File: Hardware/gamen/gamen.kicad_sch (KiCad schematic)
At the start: 1 part, among them U1 STM32H743IGTx

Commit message: Gamen: Power supply done and mcu basics done in shcems with minor fix in shori
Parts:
- removed U1: STM32H743IGTx, Package_QFP:LQFP-176_24x24mm_P0.5mm, symbol MCU_ST_STM32H7:STM32H743IGTx
- added C1, C2, C24, C25: 10uF, symbol Device:C
- added C10, C11, C13, C14, C15, C16, C17, C18, C19, C20, C21, C22, C23, C26, C28, C3, C32, C7, C8, C9: 100nF, symbol Device:C
- added C12: 100nF, Capacitor_SMD:C_0402_1005Metric_Pad0.74x0.62mm_HandSolder, symbol Device:C
- added C27, C31: 1uF, symbol Device:C
- added C29, C30: 2.2uF, symbol Device:C
- added C4: 22uF, symbol Device:C
- added C5, C6: 12pF, symbol Device:C
- added J1: POWER IN, symbol Connector_Generic:Conn_01x02
- added L1: 3.3uH, symbol Device:L
- added R1: 33.2K, symbol Device:R
- added R2, R3: 10K, symbol Device:R
- added R4: 10Ω, symbol Device:R
- added RST1: SW_Push, Button_Switch_SMD:SW_SPST_B3U-1000P, symbol Switch:SW_Push
- added SW1: SW_SPDT, Connector_PinHeader_2.54mm:PinHeader_1x03_P2.54mm_Vertical, symbol Switch:SW_SPDT
- added U1: TPS562201DDCR, Package_TO_SOT_SMD:SOT-23-6, symbol My symbols:TPS62086RLTR
- added U2: STM32H743IITx, Package_QFP:LQFP-176_24x24mm_P0.5mm, symbol MCU_ST_STM32H7:STM32H743IITx
- added Y1: 25MHz, Crystal:Crystal_SMD_WE_CFPX-180-4Pin_3.2x2.5mm, symbol Device:Crystal_GND2
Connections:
- new net: C29.1, U2.125 (VCAP)
- new net: R3.1, U2.166 (BOOT0)
- new net: C30.1, U2.81 (VCAP)
- new net: C3.2, L1.1, U1.2 (SW)
- new net: C3.1, U1.6 (VBST)
- new net: R1.2, R2.1, U1.4 (VFB)
- new net +3.3V: C10.2, C11.2, C13.2, C14.2, C15.2, C16.1, C17.1, C18.1, C19.1, C20.1, C21.1, C22.1, C23.1, C24.1, C4.1, C7.2, C8.2, C9.2, L1.2, R1.1, R4.1, SW1.3 (C), U2.103 (VDD), U2.114 (VDD33_USB), U2.127 (VDD), U2.136 (VDD), U2.149 (VDD), U2.15 (VDD), U2.159 (VDD), U2.172 (VDD), U2.23 (VDD), U2.36 (VDD), U2.49 (VDD), U2.6 (VBAT), U2.62 (VDD), U2.72 (VDD), U2.82 (VDD), U2.91 (VDD)
- new net +3.3VA: C25.1, C26.1, C27.1, C28.1, C31.1, C32.1, R4.2, U2.38 (VREF+), U2.39 (VDDA)
- new net +5V: C1.1, C2.1, J1.2 (Pin_2), U1.3 (VIN), U1.5 (EN)
- new net BOOT0_R_TO_SW: R3.2, SW1.2 (B)
- new net GND: C1.2, C10.1, C11.1, C12.2, C13.1, C14.1, C15.1, C16.2, C17.2, C18.2, C19.2, C2.2, C20.2, C21.2, C22.2, C23.2, C24.2, C25.2, C26.2, C27.2, C28.2, C29.2, C30.2, C31.2, C32.2, C4.2, C5.2, C6.2, C7.1, C8.1, C9.1, J1.1 (Pin_1), R2.2, RST1.2, SW1.1 (A), U1.1 (GND), U2.102 (VSS), U2.113 (VSS), U2.126 (VSS), U2.135 (VSS), U2.14 (VSS), U2.148 (VSS), U2.158 (VSS), U2.22 (VSS), U2.37 (VSSA), U2.48 (VSS), U2.61 (VSS), U2.71 (VSS), U2.90 (VSS), Y1.2
- new net NRST: C12.1, RST1.1, U2.31 (NRST)
- new net OSC_IN: C5.1, U2.29 (PH0), Y1.3
- new net OSC_OUT: C6.1, U2.30 (PH1), Y1.1
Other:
- note added: "POWER SUPPLY"

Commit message: GAMEN: Started SDRAM
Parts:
- added C33: 100nF, Capacitor_SMD:C_0402_1005Metric_Pad0.74x0.62mm_HandSolder, symbol Device:C
- added C34, C35, C36, C37, C38, C39, C40, C41, C42: 100nF, symbol Device:C
- added C43: 10uF, symbol Device:C
- added J2: Conn_01x05_Pin, Connector_Molex:Molex_PicoBlade_53048-0510_1x05_P1.25mm_Horizontal, symbol Connector:Conn_01x05_Pin
- added J3: UART_Header, MyFootprints:CONN04_530480410_MOL, symbol Connector:Conn_01x04_Pin
- added U14: (no value), Package_TO_SOT_SMD:SOT-23, symbol MyCrystal:ESDS452DBZRQ1
- added U3: AS4C16M16SA-6TIN, Package_SO:TSOP-II-54_22.2x10.16mm_P0.8mm, symbol My symbols:AS4C16M16SA-6TIN
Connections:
- net +3.3V: now also C33.1, C34.1, C35.2, C36.2, C37.2, C38.2, C39.2, C40.2, C41.2, C42.2, C43.2, J2.5 (Pin_5), J3.1 (Pin_1), U3.1 (VDD), U3.14 (VDD), U3.27 (VDD), U3.3 (VDDQ), U3.43 (VDDQ), U3.49 (VDDQ), U3.9 (VDDQ)
- net GND: now also C33.2, C34.2, C35.1, C36.1, C37.1, C38.1, C39.1, C40.1, C41.1, C42.1, C43.1, J2.1 (Pin_1), J3.4 (Pin_4), U14.3 (GND), U3.12 (VSSQ), U3.28 (VSS), U3.41 (VSS), U3.46 (VSSQ), U3.52 (VSSQ), U3.54 (VSS), U3.6 (VSSQ)
- net NRST: now also J2.2 (Pin_2)
- net SWDIO: now reaches U2.124 (PA13)
- net SWDIO: now also J2.4 (Pin_4)
- net SWCLK: now reaches U2.137 (PA14)
- net SWCLK: now also J2.3 (Pin_3)
- net BOOT0: now reaches R3.1, U2.166 (BOOT0)
- new net SDRAM_DQ0: U3.2 (DQ0)
- new net UART_RX: J3.2 (Pin_2), U14.2 (IO2)
- new net UART_TX: J3.3 (Pin_3)
- no-connect marks 0 -> 1
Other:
- note added: "UART SWITCH ON GAMEN"
- moved on the sheet: C10, C11, C12, C13, C14, C15, C16, C17, C18, C19, C20, C21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

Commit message: Gamen: Screen FPC connector added
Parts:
- added C44: 10uF, symbol Device:C
- added C45: 100nF, symbol Device:C
- added J4: MIDI CONN, Connector_Molex:Molex_PicoBlade_53048-0210_1x02_P1.25mm_Horizontal, symbol Connector_Generic:Conn_01x02
- added J5: SCREEN CONN, symbol Connector_Generic:Conn_01x40
- added R5: 220Ω, symbol Device:R
- added U4: W25Q256JWPIQ, Package_SON:WSON-8-1EP_6x5mm_P1.27mm_EP3.4x4.3mm, symbol Memory_Flash:W25Q128JVP
- added U6: (no value), Package_TO_SOT_SMD:SOT-23, symbol MyCrystal:ESDS452DBZRQ1
- added U7: TLP2361(E, Package_SO:SO-5-6_4.55x3.7mm_P1.27mm, symbol Isolator:TLP2310
- renumbered U14 to U5
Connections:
- net +3.3V: now also C44.2, C45.2, J5.4 (Pin_4), U4.8 (VCC), U7.6 (VDD)
- net +5V: now also J5.1 (Pin_1), J5.2 (Pin_2), U6.1 (IO1), U6.2 (IO2)
- net GND: now also C44.1, C45.1, J5.29 (Pin_29), J5.3 (Pin_3), J5.36 (Pin_36), U4.4 (GND), U4.9 (EP), U6.3 (GND), U7.4 (GND)
- net SDRAM_DQ0: now also U2.104 (PD14), U2.142 (PD0)
- net UART_RX: now also J3.3 (Pin_3), U2.93 (PB13); no longer J3.2 (Pin_2)
- net UART_TX: now also J3.2 (Pin_2), U2.92 (PB12), U5.1 (IO1); no longer J3.3 (Pin_3)
- net SDRAM_DQ1: now reaches U2.105 (PD15)
- net SDRAM_DQ1: now also U3.4 (DQ1)
- net SDRAM_A12: now reaches U2.106 (PG2)
- net SDRAM_A12: now also U3.36 (A12)
- net SDRAM_BA0: now reaches U2.108 (PG4)
- net SDRAM_BA0: now also U3.20 (BA0)
- net SDRAM_BA1: now reaches U2.109 (PG5)
- net SDRAM_BA1: now also U3.21 (BA1)
- net SDRAM_CLK: now reaches U2.112 (PG8)
- net SDRAM_CLK: now also U3.38 (CLK)
- net SDRAM_DQ3: now reaches U2.143 (PD1)
- net SDRAM_DQ3: now also U3.7 (DQ3)
- net SDRAM_A0: now reaches U2.16 (PF0)
- net SDRAM_A0: now also U3.23 (A0)
- net SDRAM_CAS: now reaches U2.160 (PG15)
- net SDRAM_CAS: now also U3.17 (*CAS)
- net SDRAM_NBL0: now reaches U2.169 (PE0)
- net SDRAM_NBL0: now also U3.15 (LDQM)
- net SDRAM_A1: now reaches U2.17 (PF1)
- net SDRAM_A1: now also U3.24 (A1)
- net SDRAM_NBL1: now reaches U2.170 (PE1)
- net SDRAM_NBL1: now also U3.39 (UDQM)
- net SDRAM_A2: now reaches U2.18 (PF2)
- net SDRAM_A2: now also U3.25 (A2)
- net SDRAM_A3: now reaches U2.19 (PF3)
- net SDRAM_A3: now also U3.26 (A3)
- net SDRAM_A4: now reaches U2.20 (PF4)
- net SDRAM_A4: now also U3.29 (A4)
- net SDRAM_A5: now reaches U2.21 (PF5)
- net SDRAM_A5: now also U3.30 (A5)
- net QSPI_IO3: now reaches U2.24 (PF6)
- net QSPI_IO3: now also U4.7 (~{HOLD}/~{RESET}/IO_{3})
- net QSPI_IO2: now reaches U2.25 (PF7)
- net QSPI_IO2: now also U4.3 (~{WP}/IO_{2})
- net QSPI_IO1: now reaches U2.26 (PF8)
- net QSPI_IO1: now also U4.2 (DO/IO_{1})
- net QSPI_IO0: now reaches U2.27 (PF9)
- net QSPI_IO0: now also U4.5 (DI/IO_{0})
- net QSPI_CLK: now reaches U2.28 (PF10)
- net QSPI_CLK: now also U4.6 (CLK)
- net SDRAM_WE: now reaches U2.32 (PC0)
- net SDRAM_WE: now also U3.16 (*WE)
- net SDRAM_CS: now reaches U2.34 (PC2_C)
- net SDRAM_CS: now also U3.19 (*CS)
- net SDRAM_CKE: now reaches U2.35 (PC3_C)
- net SDRAM_CKE: now also U3.37 (CKE)
- net SDNIS_RAS: now reaches U2.59 (PF11)
- net SDNIS_RAS: now also U3.18 (*RAS)
- net SDRAM_A6: now reaches U2.60 (PF12)
- net SDRAM_A6: now also U3.31 (A6)
- net SDRAM_A7: now reaches U2.63 (PF13)
- net SDRAM_A7: now also U3.32 (A7)
- net SDRAM_A8: now reaches U2.64 (PF14)
- net SDRAM_A8: now also U3.33 (A8)
- net SDRAM_A9: now reaches U2.65 (PF15)
- net SDRAM_A9: now also U3.34 (A9)
- net SDRAM_A10: now reaches U2.66 (PG0)
- net SDRAM_A10: now also U3.22 (A10/AP)
- net SDRAM_A11: now reaches U2.67 (PG1)
- net SDRAM_A11: now also U3.35 (A11)
- net SDRAM_DQ6: now reaches U2.68 (PE7)
- net SDRAM_DQ6: now also U3.11 (DQ6)
- net SDRAM_DQ5: now reaches U2.69 (PE8)
- net SDRAM_DQ5: now also U3.10 (DQ5)
- net SDRAM_DQ4: now reaches U2.70 (PE9)
- net SDRAM_DQ4: now also U3.8 (DQ4)
- net SDRAM_DQ7: now reaches U2.73 (PE10)
- net SDRAM_DQ7: now also U3.13 (DQ7)
- net SDRAM_DQ8: now reaches U2.74 (PE11)
- net SDRAM_DQ8: now also U3.42 (DQ8)
- net SDRAM_DQ9: now reaches U2.75 (PE12)
- net SDRAM_DQ9: now also U3.44 (DQ9)
- net SDRAM_DQ10: now reaches U2.76 (PE13)
- net SDRAM_DQ10: now also U3.45 (DQ10)
- net SDRAM_DQ11: now reaches U2.77 (PE14)
- net SDRAM_DQ11: now also U3.47 (DQ11)
- net SDRAM_DQ12: now reaches U2.78 (PE15)
- net SDRAM_DQ12: now also U3.48 (DQ12)
- net SDRAM_DQ13: now reaches U2.96 (PD8)
- net SDRAM_DQ13: now also U3.50 (DQ13)
- net SDRAM_DQ14: now reaches U2.97 (PD9)
- net SDRAM_DQ14: now also U3.51 (DQ14)
- net SDRAM_DQ15: now reaches U2.98 (PD10)
- net SDRAM_DQ15: now also U3.53 (DQ15)
- net SDRAM_DQ2: now reaches U3.5 (DQ2)
- new net: R5.2, U7.1 (A)
- new net MIDI_GND: J4.1 (Pin_1), U7.3 (K)
- new net MIDI_OUT: U7.5 (VO)
- new net QSPI_CS: U4.1 (~{CS})
- new net SCREEN_B0: J5.21 (Pin_21)
- new net SCREEN_B1: J5.22 (Pin_22)
- new net SCREEN_B2: J5.23 (Pin_23)
- new net SCREEN_B3: J5.24 (Pin_24)
- new net SCREEN_B4: J5.25 (Pin_25)
- new net SCREEN_B5: J5.26 (Pin_26)
- new net SCREEN_B6: J5.27 (Pin_27)
- new net SCREEN_B7: J5.28 (Pin_28)
- new net SCREEN_CAP_INT: J5.40 (Pin_40)
- new net SCREEN_CAP_RST: J5.39 (Pin_39)
- new net SCREEN_CLK: J5.30 (Pin_30)
- new net SCREEN_DE: J5.34 (Pin_34)
- new net SCREEN_DISP: J5.31 (Pin_31)
- new net SCREEN_G0: J5.13 (Pin_13)
- new net SCREEN_G1: J5.14 (Pin_14)
- new net SCREEN_G2: J5.15 (Pin_15)
- new net SCREEN_G3: J5.16 (Pin_16)
- new net SCREEN_G4: J5.17 (Pin_17)
- new net SCREEN_G5: J5.18 (Pin_18)
- new net SCREEN_G6: J5.19 (Pin_19)
- new net SCREEN_G7: J5.20 (Pin_20)
- new net SCREEN_HSYNC: J5.32 (Pin_32)
- new net SCREEN_I2C_SCL: J5.38 (Pin_38)
- new net SCREEN_I2C_SDA: J5.37 (Pin_37)
- new net SCREEN_PWM: J5.35 (Pin_35)
- new net SCREEN_R0: J5.5 (Pin_5)
- new net SCREEN_R1: J5.6 (Pin_6)
- new net SCREEN_R2: J5.7 (Pin_7)
- new net SCREEN_R3: J5.8 (Pin_8)
- new net SCREEN_R4: J5.9 (Pin_9)
- new net SCREEN_R5: J5.10 (Pin_10)
- new net SCREEN_R6: J5.11 (Pin_11)
- new net SCREEN_R7: J5.12 (Pin_12)
- new net SCREEN_VSYNC: J5.33 (Pin_33)
- new net SLEVE: J4.2 (Pin_2), R5.1
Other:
- note added: "EXTERNAL RAM AND FLASH"
- note added: "MICROCONTROLLER"
- note added: "MIDI CONN + OPTOCOUPLER"
- note removed: "UART SWITCH ON GAMEN"
- moved on the sheet: C10, C11, C12, C13, C14, C15, C16, C17, C18, C19, C20, C21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

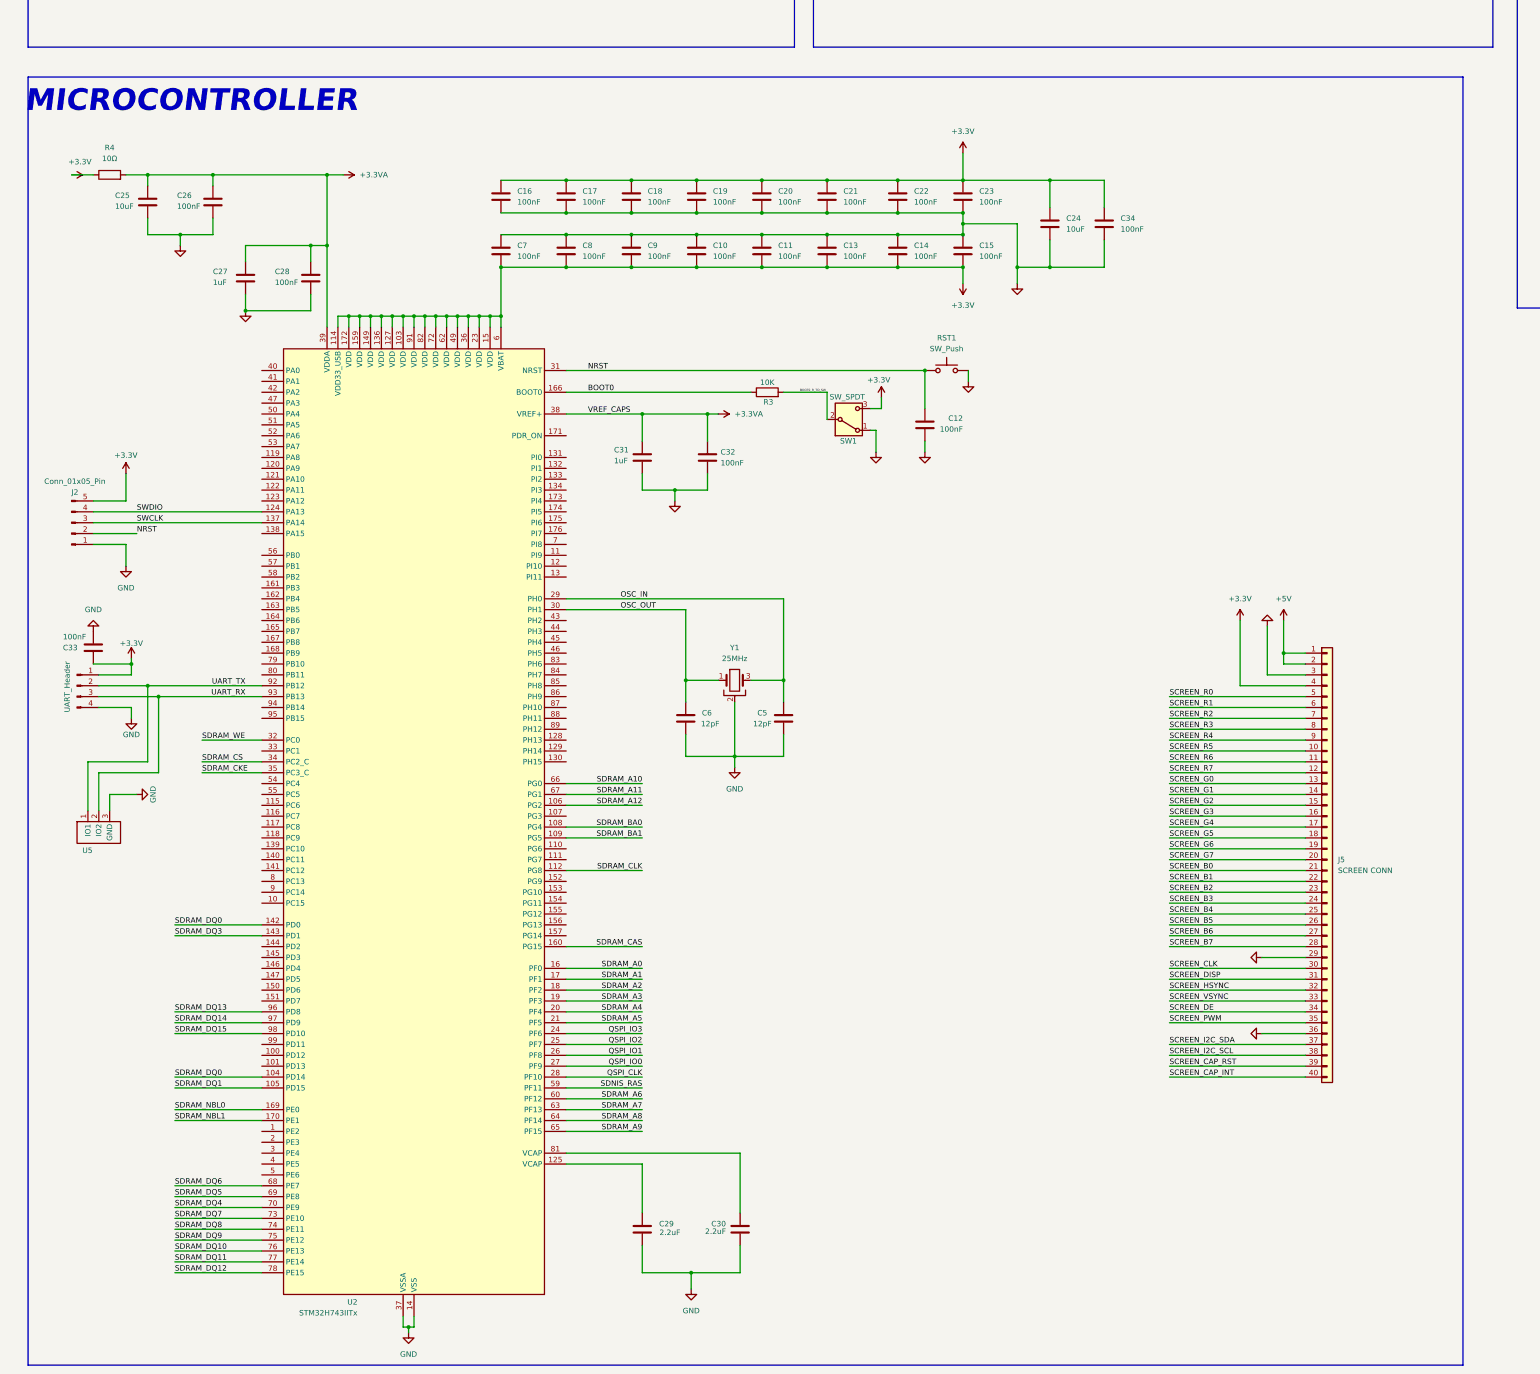
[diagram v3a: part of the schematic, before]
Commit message: Gamen: Screen connected to mcu
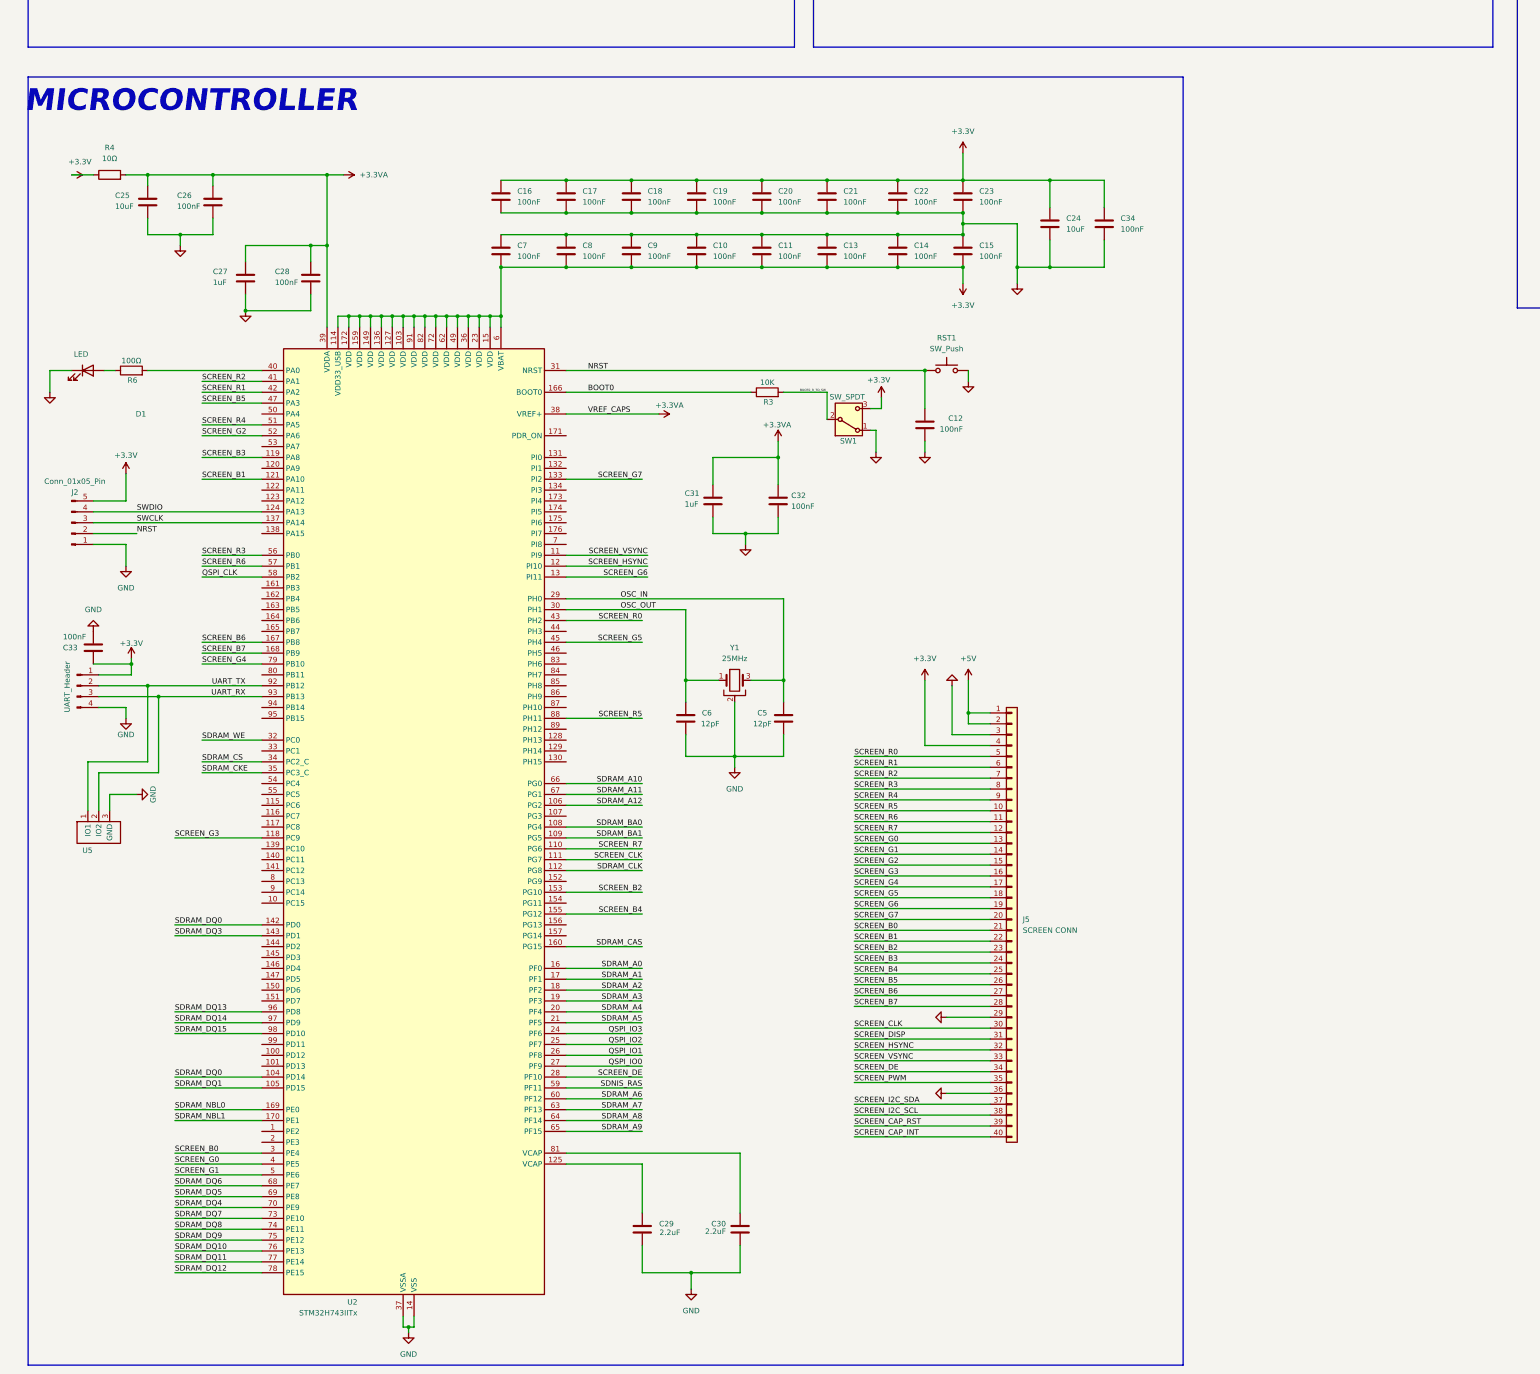
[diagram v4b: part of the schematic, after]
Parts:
- added D1: LED, symbol Device:LED
- added R6: 100Ω, symbol Device:R
- J5: footprint (none) -> My footprints:HARWIN_M58-2800342R
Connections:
- net GND: now also D1.1 (K)
- net QSPI_CLK: now also U2.58 (PB2); no longer U2.28 (PF10)
- net SCREEN_B0: now also U2.3 (PE4)
- net SCREEN_B1: now also U2.121 (PA10)
- net SCREEN_B2: now also U2.153 (PG10)
- net SCREEN_B3: now also U2.119 (PA8)
- net SCREEN_B4: now also U2.155 (PG12)
- net SCREEN_B5: now also U2.47 (PA3)
- net SCREEN_B6: now also U2.167 (PB8)
- net SCREEN_B7: now also U2.168 (PB9)
- net SCREEN_CLK: now also U2.111 (PG7)
- net SCREEN_DE: now also U2.28 (PF10)
- net SCREEN_G0: now also U2.4 (PE5)
- net SCREEN_G1: now also U2.5 (PE6)
- net SCREEN_G2: now also U2.52 (PA6)
- net SCREEN_G3: now also U2.118 (PC9)
- net SCREEN_G4: now also U2.79 (PB10)
- net SCREEN_G5: now also U2.45 (PH4)
- net SCREEN_G6: now also U2.13 (PI11)
- net SCREEN_G7: now also U2.133 (PI2)
- net SCREEN_HSYNC: now also U2.12 (PI10)
- net SCREEN_R0: now also U2.43 (PH2)
- net SCREEN_R1: now also U2.42 (PA2)
- net SCREEN_R2: now also U2.41 (PA1)
- net SCREEN_R3: now also U2.56 (PB0)
- net SCREEN_R4: now also U2.51 (PA5)
- net SCREEN_R5: now also U2.88 (PH11)
- net SCREEN_R6: now also U2.57 (PB1)
- net SCREEN_R7: now also U2.110 (PG6)
- net SCREEN_VSYNC: now also U2.11 (PI9)
- net at U2.40 (PA0): now also R6.2
- new net: D1.2 (A), R6.1
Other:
- moved on the sheet: C31, C32, J5
